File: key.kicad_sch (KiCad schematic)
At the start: 2 parts

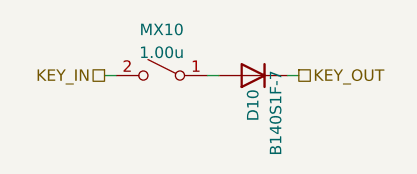
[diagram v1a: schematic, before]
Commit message: g915 and k618 pcb key and cutout placement
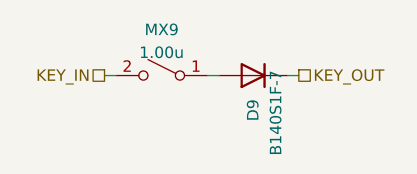
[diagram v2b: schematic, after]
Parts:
- MX9: renamed from MX10; footprint key-switches:SW_Gateron_LowProfile_HotSwap_PTH -> key-switches:SW_Kailh_Choc_V1_THT
- renumbered D10 to D9

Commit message: Minor pcb layout changes. Add matrix led drivers
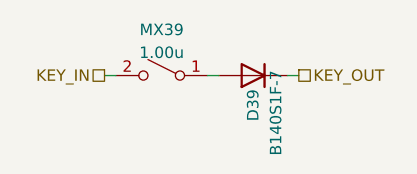
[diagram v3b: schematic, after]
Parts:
- renumbered D9 to D39, MX9 to MX39
